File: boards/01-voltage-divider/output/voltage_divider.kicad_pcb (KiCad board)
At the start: 2 copper layers, 30 x 25 mm, 4 parts, among them J1 IN, J2 OUT

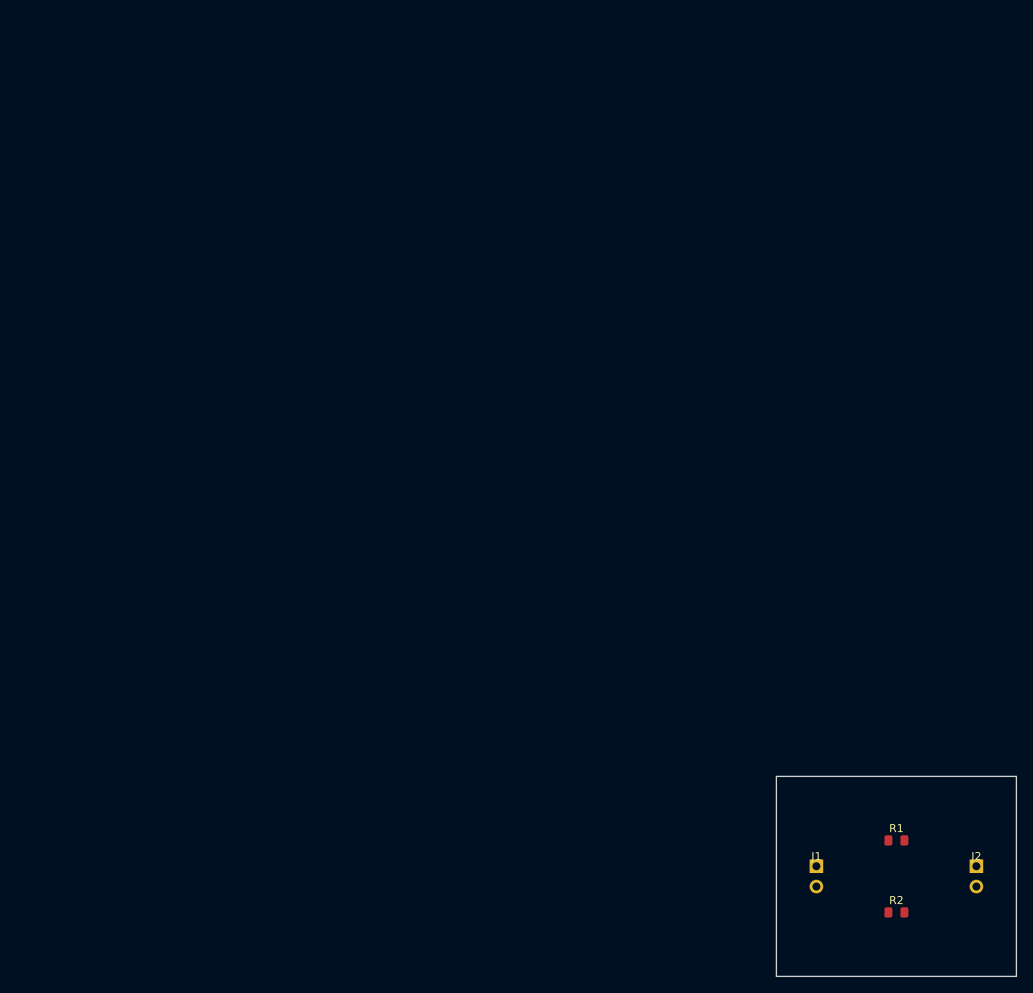
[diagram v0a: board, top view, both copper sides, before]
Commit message: feat(pcb): add page_fit to size sheet to board + center, apply to all boards
Add PCB.page_fit(margin=5.0) which rewrites the (paper ...) node to a tight
(paper "User" W H) sized to the Edge.Cuts bbox plus a uniform margin and
translates every board item (footprints, segments, vias, zones incl.
filled_polygons, gr_* graphics, text) so the board is centered with that
margin. Pure geometric translate — relative geometry, routing and DRC
validity are preserved, no re-route needed.

Expose it as `kct pcb page-fit <pcb> [-o out] [--margin] [--dry-run]` and
wire a PAGE_FIT build step (after stitch, before verify/export) so future
boards are centered too. Apply page_fit to all demo boards (00-07 +
external/softstart), both routed and unrouted PCBs, so the committed
layouts fill + center the KiCanvas viewer instead of sitting tiny in an A4
page. Boards 00/01 stay DRC-clean (0 errors); no board's DRC count changed.

Co-Authored-By: Claude Opus 4.7 <noreply@anthropic.com>
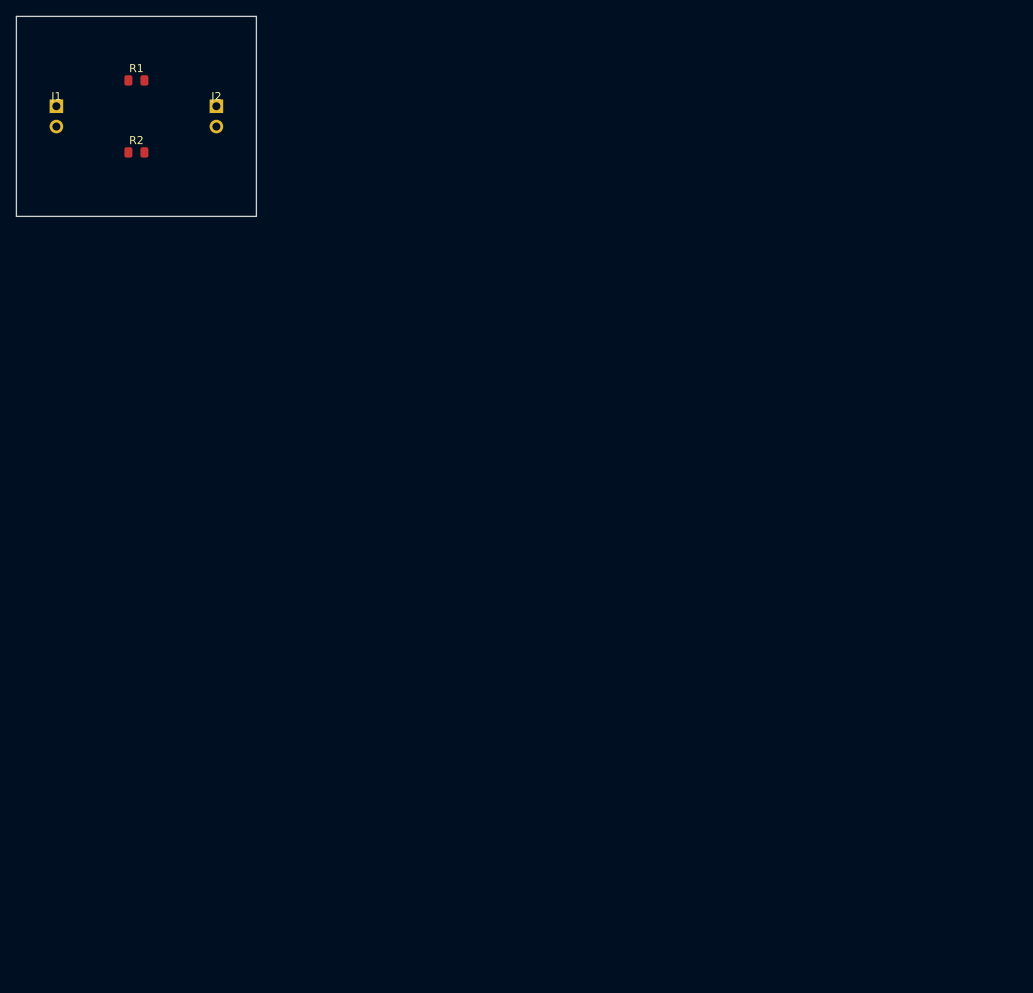
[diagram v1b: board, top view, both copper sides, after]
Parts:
- moved J1 134.4 mm to (10.0, 17.5)
- moved J2 134.4 mm to (30.0, 17.5)
- moved R1 134.4 mm to (20.0, 13.0)
- moved R2 134.4 mm to (20.0, 22.0)

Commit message: fix(pcb): page-fit routed boards only; revert unrouted sources (refs #3714)
page_fit was applied to and committed for the UNROUTED board sources too.
Because the autorouter is absolute-grid-position-dependent, translating the
unrouted boards changed routing outcomes and turned CI red on three jobs:
- Test: board-02 re-route produced a platform-specific segment count.
- Diff-Pair (06) / Match-Group (07): re-routing the moved unrouted boards
  fractured plane nets under the copper-union pour audit (#3509/#3617).

page_fit is a pure post-route translation, so it must touch the ROUTED
output only:
- Revert every unrouted boards/*/output/<name>.kicad_pcb to origin/main
  (byte-identical); keep the page-fitted *_routed.kicad_pcb (gallery/viewer).
- Revert tests/router/test_board02_manufacturable_baseline.py to main
  (unrouted board-02 unchanged -> reproduces main's result).
- Build hook: _run_step_page_fit now operates on the routed PCB only and
  skips cleanly when no routed output exists, instead of falling back to and
  persisting a page-fit unrouted PCB.

Retains the sound geometry fixes (translation-invariant
point_to_segment_distance, _format_coord_mm, diffpair +1e-6 window tolerance).

Co-Authored-By: Claude Opus 4.7 <noreply@anthropic.com>
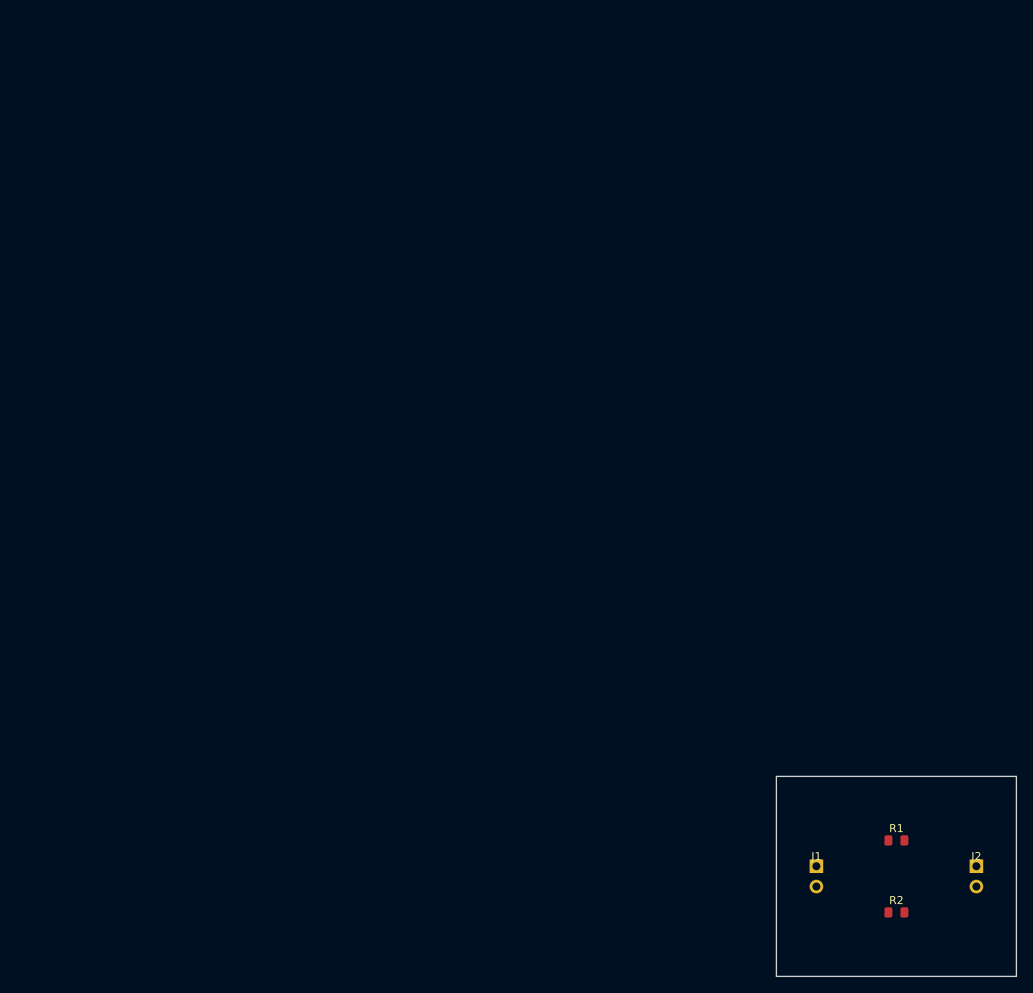
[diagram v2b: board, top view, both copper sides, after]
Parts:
- moved J1 134.4 mm to (105.0, 112.5)
- moved J2 134.4 mm to (125.0, 112.5)
- moved R1 134.4 mm to (115.0, 108.0)
- moved R2 134.4 mm to (115.0, 117.0)

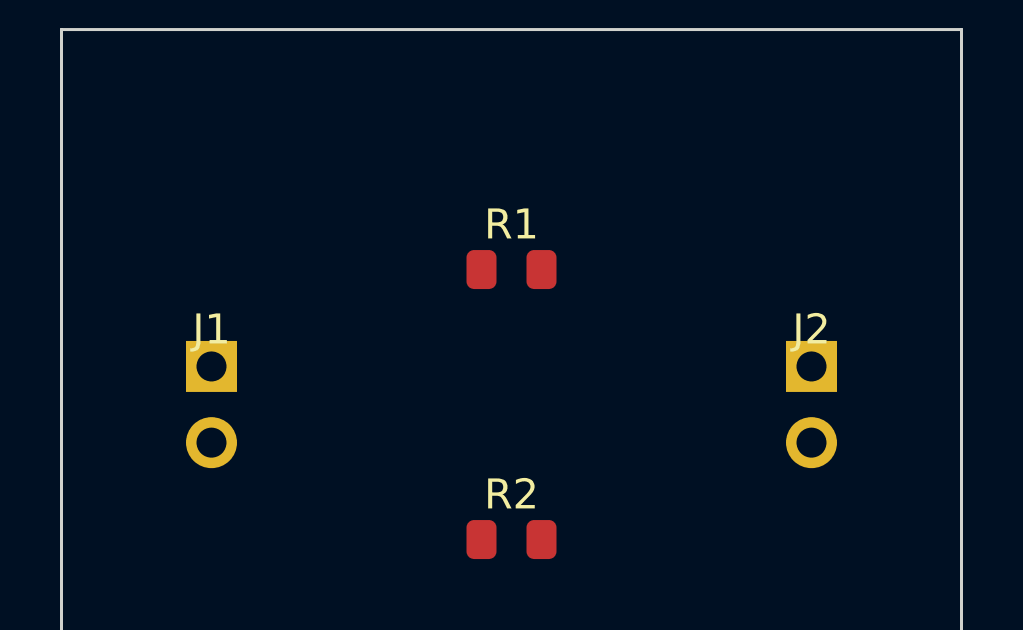
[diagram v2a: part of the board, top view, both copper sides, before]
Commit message: fix(boards): move connector refdes off pad-1 copper on boards 00/01 (#3962)
* fix(boards): move connector refdes off pad-1 copper on boards 00/01

The demo-board PCB generators for boards 00 (simple-led) and 01
(voltage-divider) hard-coded the connector refdes at local (0, -2.5),
placing the reference-designator text box over pad 1's exposed mask
aperture. Pad 1 is a 1.7x1.7 mm thru-hole centred at (0, -1.27), so its
copper top edge is at -2.12 mm; a 1x1 mm / 0.15 mm-stroke refdes has its
bottom edge 0.575 mm below centre, so -2.5 left the box inside the
aperture and fired silk_over_copper on J1/J2.

Move the connector refdes to (0, -3.5) -- the same offset the LED
footprint already uses and passes silk_over_copper -- which clears the
aperture with margin. Add a geometry-based justification in each
generate_connector docstring. The resistor refdes at (0, -1.5) was
already clear of the 0805 pads and is unchanged.

Regenerate boards 00 and 01 committed artifacts from the fixed
generators. Fresh kct check and kicad-cli pcb drc --refill-zones both
report 0 silk_over_copper (and 0 total DRC violations) on the routed
PCBs.

Remove the _SILK_PLACEMENT_RULES carve-out from
tests/test_board_01_ship_ready.py so the strict 0-warning gate holds
unconditionally, and move board 01 from the silk_over_copper positive
fixture to the clean-board list in tests/test_validate_silkscreen.py.

Closes #3939

Co-Authored-By: Claude Fable 5 <noreply@anthropic.com>

* fix(board-01): restore #3715 page-fit on regenerated routed artifact

The generator-only regen dropped the PAGE_FIT post-pass that produced
main's committed truth, reverting (paper "User" 40 35) -> (paper "A4")
and un-centering the board from ~10-30mm back to a full-A4 ~105-125mm
layout, silently undoing the #3715 gallery-centering.

Re-ran the routed artifact through the same pipeline main uses:
`kct pcb page-fit --margin 5.0` after routing, then regenerated the
JLCPCB manufacturing bundle from the page-fit board.

Verification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
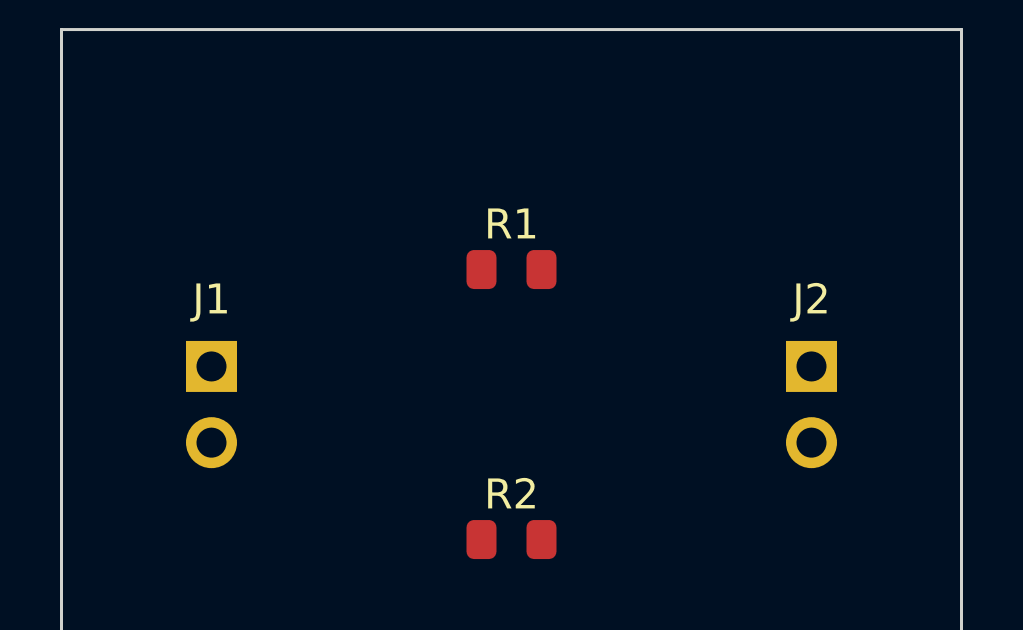
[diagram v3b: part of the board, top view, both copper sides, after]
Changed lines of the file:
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@@
     (layer "F.Cu")
     (at 105.0 112.5)
-    (fp_text reference "J1" (at 0 -2.5) (layer "F.SilkS")
+    (fp_text reference "J1" (at 0 -3.5) (layer "F.SilkS")
       (effects (font (size 1 1) (thickness 0.15)))
     )
@@
     (layer "F.Cu")
     (at 125.0 112.5)
-    (fp_text reference "J2" (at 0 -2.5) (layer "F.SilkS")
+    (fp_text reference "J2" (at 0 -3.5) (layer "F.SilkS")
       (effects (font (size 1 1) (thickness 0.15)))
     )
